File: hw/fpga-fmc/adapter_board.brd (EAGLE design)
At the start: 68.9 x 85.5 mm, 175 parts, among them IC1 M24C02, J1 5569262-1, J2 ASP-134488-01, U1 ADM3066E, U10 ADM3066E, U11 ADM3066E, U12 ADM3066E, U13 ADM3066E, U14 ADM3066E, U15 ADM3066E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

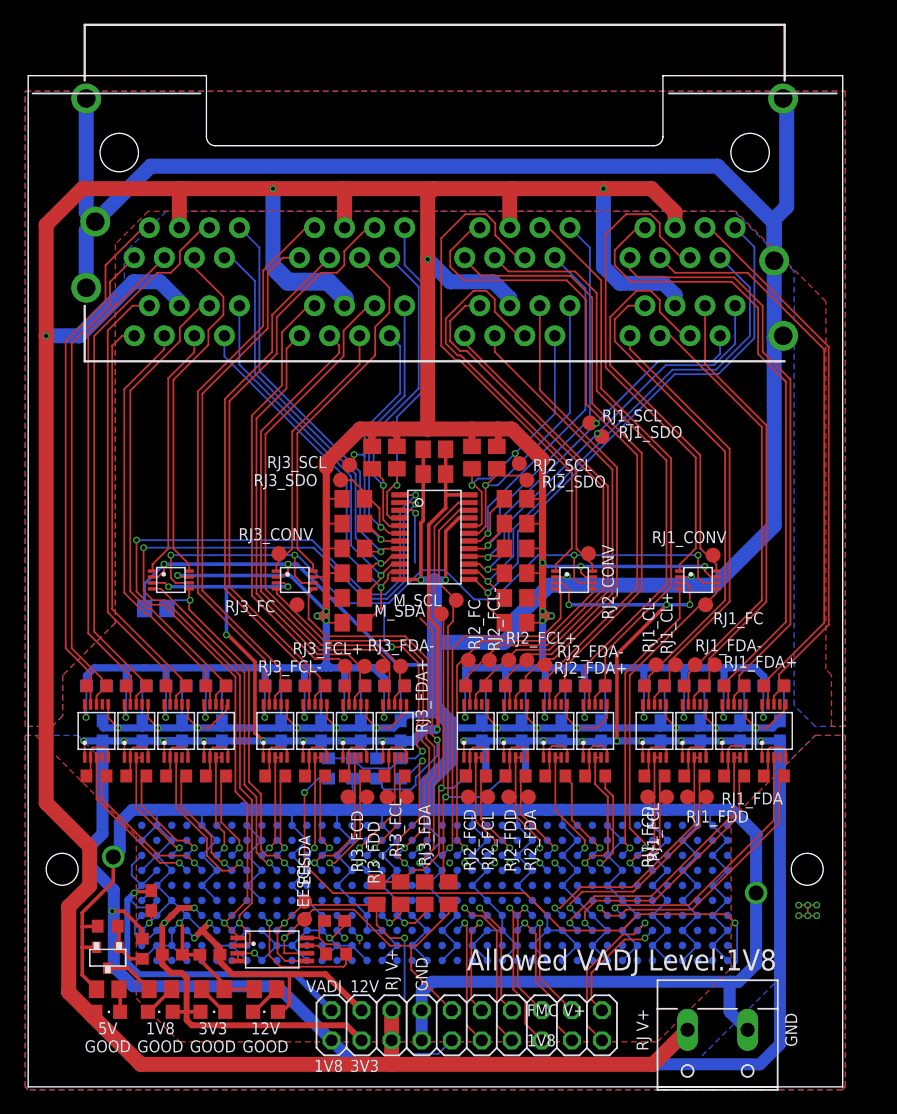
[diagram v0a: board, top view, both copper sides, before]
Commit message: hw/fpga-fmc: reposition i2c switch
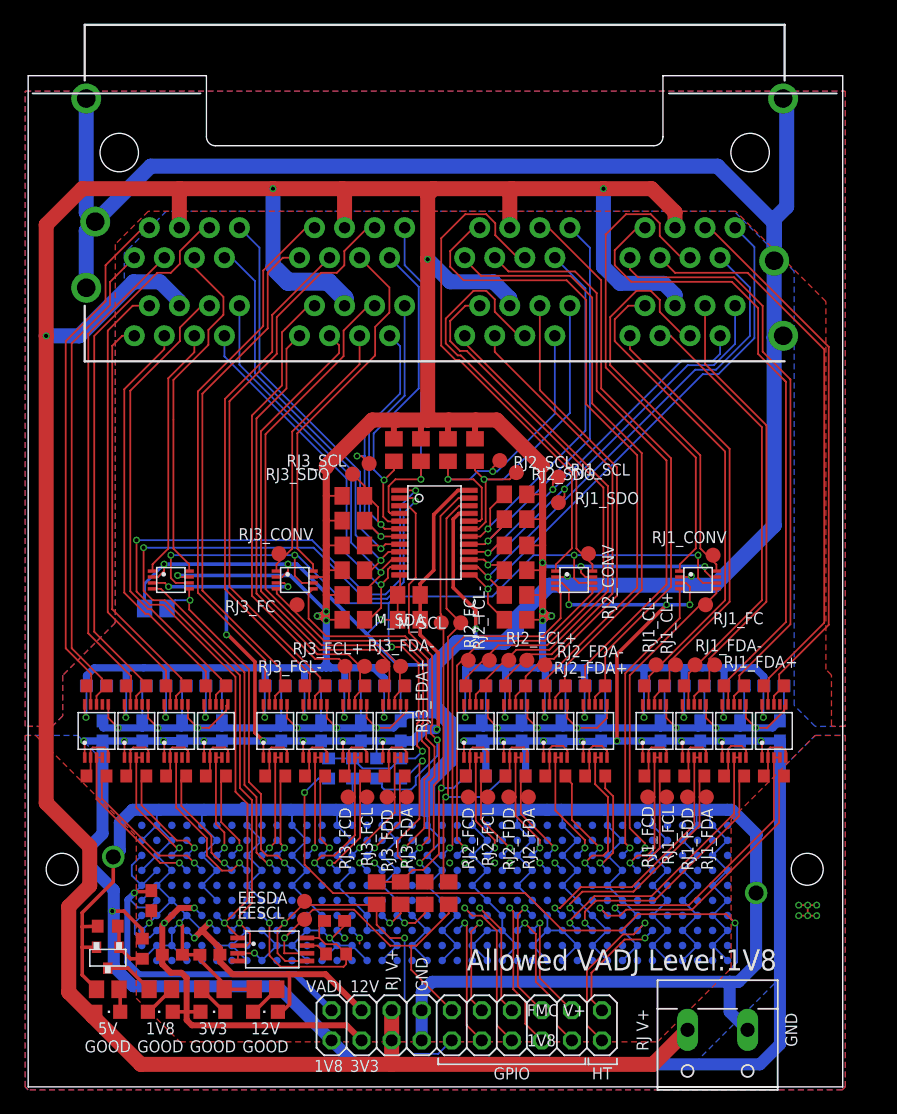
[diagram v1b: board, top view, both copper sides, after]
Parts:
- moved C3 14.6 mm to (32.3, 39.5)
- moved C4 10.4 mm to (32.3, 41.6)
- moved RJ1_SDO 6.69 mm to (45.0, 49.4)
- moved RJ1_SCL 5.29 mm to (45.0, 51.6)
- moved R21 2.13 mm to (35.6, 53.8)
- moved R3 2.13 mm to (33.3, 53.8)
- moved R4 1.95 mm to (31.1, 53.8)
- moved R20 1.95 mm to (37.9, 53.8)
- moved M_SCL 1.94 mm to (36.7, 39.2)
- moved RJ2_SCL 1.67 mm to (40.0, 53.0)
- moved RJ3_SCL 1.66 mm to (29.0, 52.7)
- moved RJ3_SDO 1.14 mm to (27.6, 51.8)
- moved RJ2_SDO 1.09 mm to (41.4, 51.9)
- moved M_SDA 0.76 mm to (35.1, 39.2)
- moved R18 0.38 mm to (41.3, 48.0)
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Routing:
- net 0V: track 811.0 -> 802.8 mm
- net FMC_LA20_P: track 37.2 -> 42.7 mm, vias 3 -> 2
- net RJ2_SCL: track 23.4 -> 27.6 mm
- net 1V8: track 284.1 -> 280.6 mm
- net CONV_OE: track 87.9 -> 85.7 mm
- net RJ5_SDO: track 48.2 -> 46.6 mm
- net RJ5_SCL: track 43.7 -> 42.3 mm
- net RJ3_SDO: track 28.7 -> 27.6 mm
- net RJ7_SDO: track 28.9 -> 29.7 mm
- net RJ1_SCL: track 33.5 -> 32.8 mm
- net RJ4_SCL: track 32.9 -> 33.5 mm
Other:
- board text added: "GPIO"
- board text added: "HT"

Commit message: hw/fpga-fmc: optimize routing
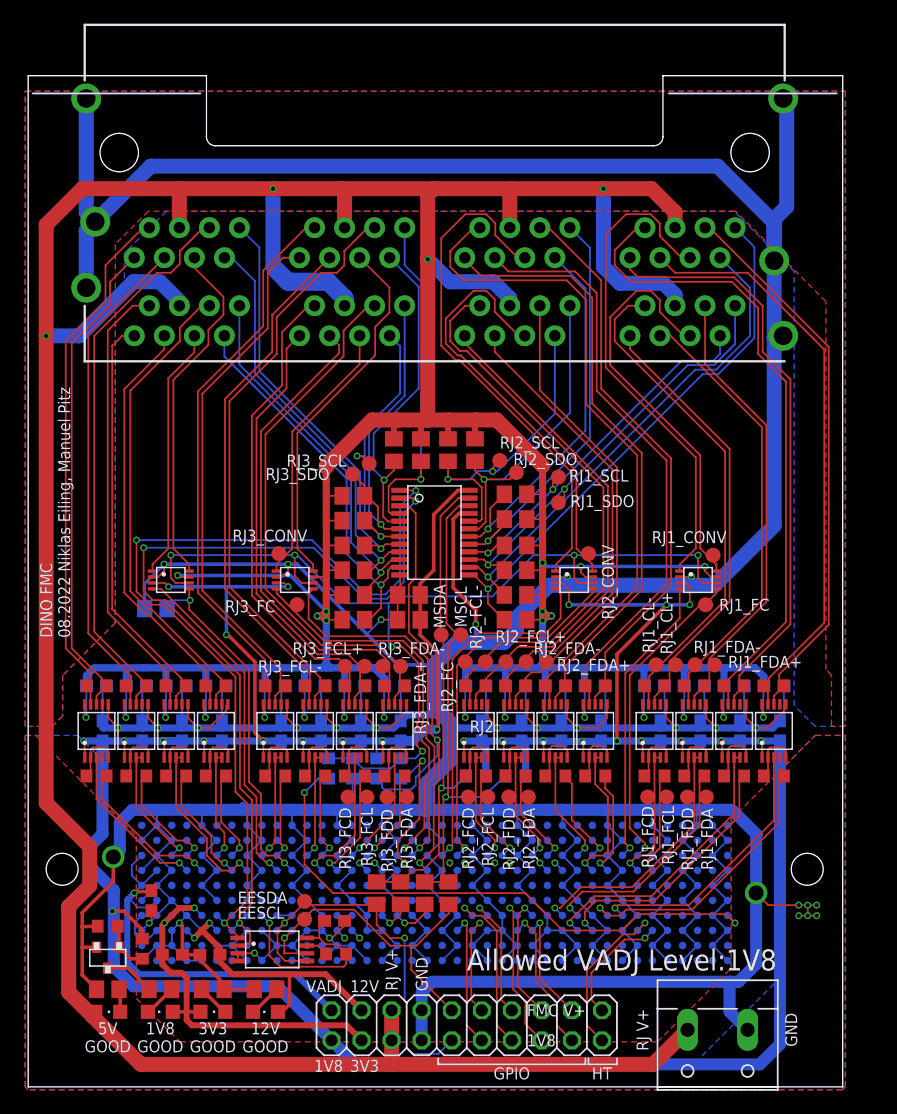
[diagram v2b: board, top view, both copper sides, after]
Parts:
- removed M_SCL, M_SDA: TPB1,27, testpad:B1,27
- added MSCL, MSDA: TPB1,27, testpad:B1,27
- R63, R64: value 0R -> 0R DNP
- R65, R66: value 0R DNP -> 0R
- moved RJ2_FCL- 0.34 mm to (38.8, 35.9), turned to 90 degrees
- moved RJ2_FDA+ 0.28 mm to (43.9, 35.9)
- moved RJ2_FCL+ 0.28 mm to (40.5, 35.9)
- moved RJ2_FC 0.28 mm to (37.1, 35.9)
- moved RJ2_FDA- 0.14 mm to (42.2, 35.9)
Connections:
- net I2C_SCL: now also MSCL.TP; no longer M_SCL.TP
- net I2C_SDA: now also MSDA.TP; no longer M_SDA.TP
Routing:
- net 0V: track 802.8 -> 811.1 mm
- net 1V8_POWER_GOOD: track 53.4 -> 49.1 mm
- net I2C_SCL: track 40.1 -> 42.2 mm
- net FMC_TDI_TDO: track 0.00 -> 1.27 mm
- net 5V: track 524.8 -> 523.7 mm
- net RJ7_DATA_N: track 45.3 -> 44.7 mm
- net LSIO5: track 5.20 -> 4.63 mm
- net RJ7_CLK_N: track 47.9 -> 47.3 mm
- net FMC_LA15_N: track 30.7 -> 30.2 mm
- net FMC_LA31_P: track 13.8 -> 14.3 mm
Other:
- board text added: "DINO FMC 08.2022 Niklas Eiling, Manuel Pitz"
- board text added: "RJ2"

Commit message: hw/fmc minor cleanup in layout and schematic
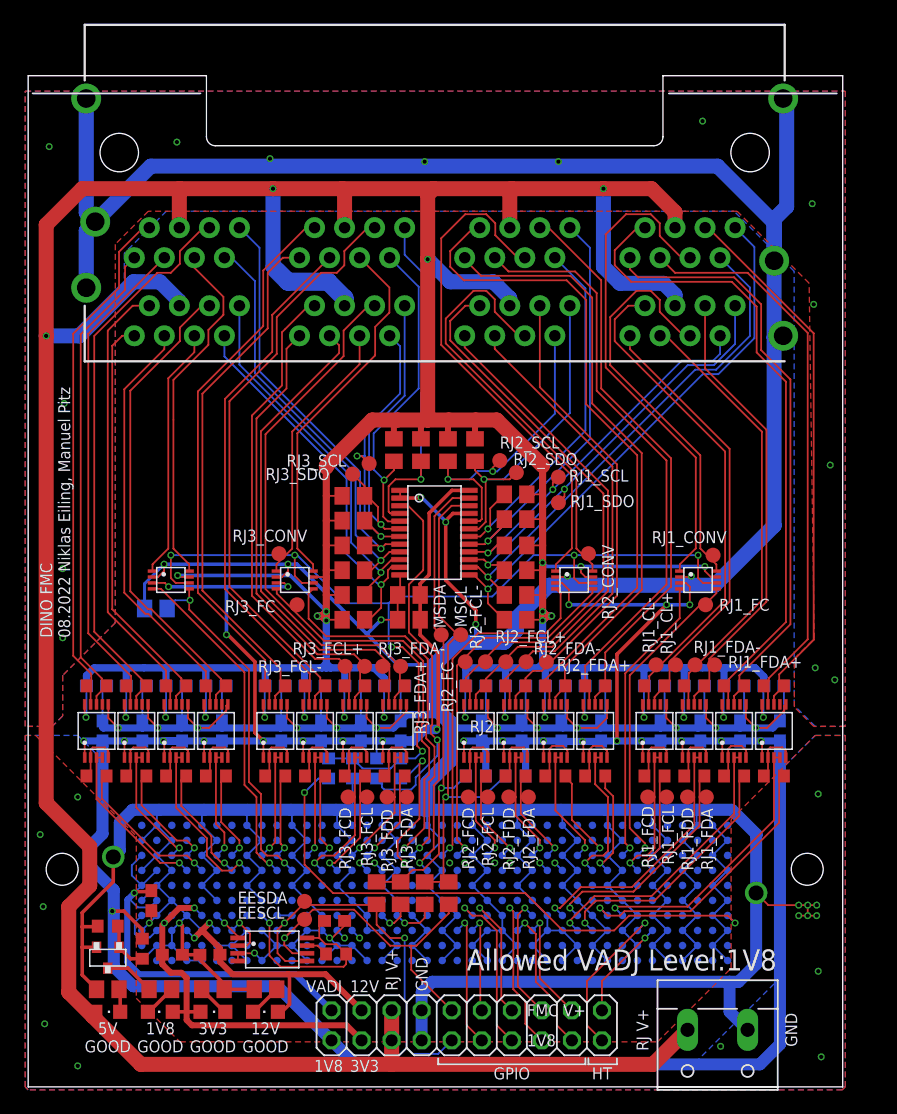
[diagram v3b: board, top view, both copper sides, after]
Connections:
- net 0V: now also U17.P0, U17.P1
- net GA0: no longer U17.P1
- net GA1: no longer U17.P0
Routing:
- net GA1: track 74.5 -> 2.66 mm, vias 3 -> 1
- net GA0: track 73.7 -> 4.05 mm, vias 3 -> 1
- net 0V: track 811.1 -> 813.4 mm, vias 28 -> 53
- net FMC_DP0_M2C_P: track 10.2 -> 8.52 mm
- net 1V8: track 280.7 -> 279.1 mm
- net RJ5_DATA_N: track 49.4 -> 48.2 mm
- net RJ5_DATA_P: track 47.1 -> 46.0 mm
- net I2C_SCL: track 42.2 -> 43.1 mm
- net I2C_SDA: track 40.6 -> 41.3 mm
- net RJ8_CLK_P: track 41.5 -> 40.9 mm
- net FMC_LA14_P: track 8.95 -> 8.35 mm
- net FMC_LA20_P: track 42.7 -> 43.2 mm
- net RJ8_CLK_N: track 44.7 -> 44.2 mm
- net FMC_DP0_M2C_N: track 13.9 -> 13.4 mm

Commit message: hw/fpga-fmc: align GND vias
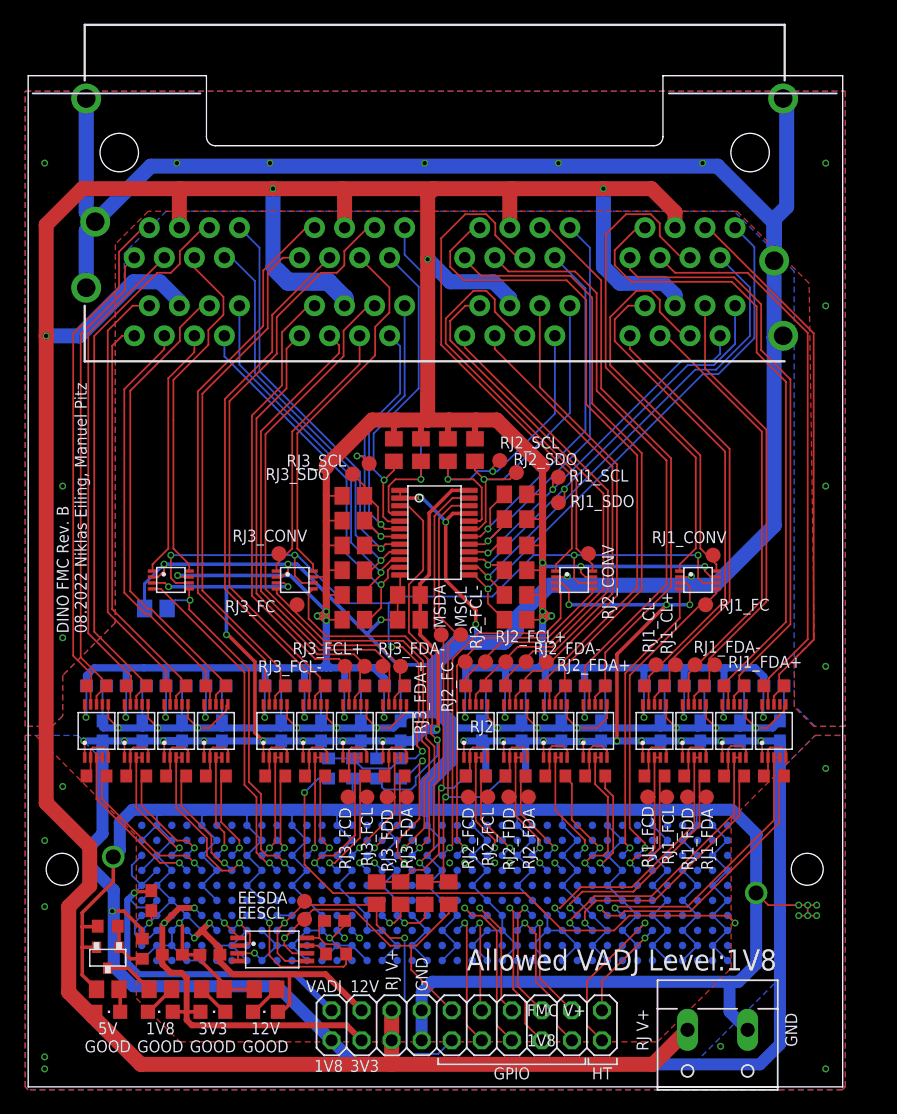
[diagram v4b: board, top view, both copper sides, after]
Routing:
- net 0V: vias 53 -> 50
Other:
- board text added: "DINO FMC Rev. B 08.2022 Niklas Eiling, Manuel Pitz"
- board text removed: "DINO FMC 08.2022 Niklas Eiling, Manuel Pitz"
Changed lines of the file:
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@@
 <wire x1="47.498" y1="1.905" x2="49.911" y2="1.905" width="0.1524" layer="21"/>
 <wire x1="49.911" y1="1.905" x2="49.911" y2="2.413" width="0.1524" layer="21"/>
-<text x="1.143" y="37.973" size="1.016" layer="21" rot="R90" align="top-left">DINO FMC
+<text x="2.54" y="38.354" size="1.016" layer="21" rot="R90" align="top-left">DINO FMC Rev. B
 08.2022 Niklas Eiling, Manuel Pitz</text>
 <text x="38.481" y="30.48" size="1.016" layer="21" rot="R180" align="center">RJ2</text>
@@
 <wire x1="35.433" y1="47.8155" x2="33.401" y2="49.8475" width="0.3048" layer="16"/>
 <via x="35.433" y="47.752" extent="1-16" drill="0.35"/>
-<via x="1.524" y="5.334" extent="1-16" drill="0.35"/>
-<via x="4.318" y="1.778" extent="1-16" drill="0.35"/>
-<via x="1.397" y="15.24" extent="1-16" drill="0.35"/>
-<via x="1.143" y="21.336" extent="1-16" drill="0.35"/>
-<via x="4.318" y="24.511" extent="1-16" drill="0.35"/>
-<via x="3.048" y="43.815" extent="1-16" drill="0.35"/>
+<via x="1.524" y="2.54" extent="1-16" drill="0.35"/>
+<via x="1.524" y="1.524" extent="1-16" drill="0.35"/>
+<via x="1.524" y="15.24" extent="1-16" drill="0.35"/>
+<via x="1.524" y="20.828" extent="1-16" drill="0.35"/>
+<via x="3.048" y="25.4" extent="1-16" drill="0.35"/>
 <via x="3.048" y="37.973" extent="1-16" drill="0.35"/>
-<via x="3.175" y="57.785" extent="1-16" drill="0.35"/>
-<via x="1.905" y="79.502" extent="1-16" drill="0.35"/>
-<via x="12.7" y="79.883" extent="1-16" drill="0.35"/>
-<via x="20.574" y="78.486" extent="1-16" drill="0.35"/>
-<via x="33.655" y="78.232" extent="1-16" drill="0.35"/>
-<via x="44.958" y="78.232" extent="1-16" drill="0.35"/>
-<via x="57.15" y="81.661" extent="1-16" drill="0.35"/>
-<via x="66.421" y="74.676" extent="1-16" drill="0.35"/>
-<via x="68.326" y="34.417" extent="1-16" drill="0.35"/>
-<via x="66.675" y="35.433" extent="1-16" drill="0.35"/>
-<via x="67.945" y="52.578" extent="1-16" drill="0.35"/>
-<via x="66.548" y="66.167" extent="1-16" drill="0.35"/>
-<via x="66.929" y="9.779" extent="1-16" drill="0.35"/>
-<via x="66.929" y="24.765" extent="1-16" drill="0.35"/>
-<via x="67.183" y="2.54" extent="1-16" drill="0.35"/>
+<via x="3.048" y="50.8" extent="1-16" drill="0.35"/>
+<via x="1.524" y="78.105" extent="1-16" drill="0.35"/>
+<via x="12.7" y="78.105" extent="1-16" drill="0.35"/>
+<via x="20.574" y="78.105" extent="1-16" drill="0.35"/>
+<via x="33.655" y="78.105" extent="1-16" drill="0.35"/>
+<via x="44.958" y="78.105" extent="1-16" drill="0.35"/>
+<via x="57.15" y="78.105" extent="1-16" drill="0.35"/>
+<via x="67.564" y="78.105" extent="1-16" drill="0.35"/>
+<via x="67.564" y="35.56" extent="1-16" drill="0.35"/>
+<via x="67.564" y="50.8" extent="1-16" drill="0.35"/>
+<via x="67.564" y="66.04" extent="1-16" drill="0.35"/>
+<via x="67.564" y="26.924" extent="1-16" drill="0.35"/>
+<via x="67.564" y="1.524" extent="1-16" drill="0.35"/>
 <via x="58.674" y="3.429" extent="1-16" drill="0.35"/>
 </signal>

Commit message: hw/fpga-fmc: make rs485 termination resistors 0805 for better power rating
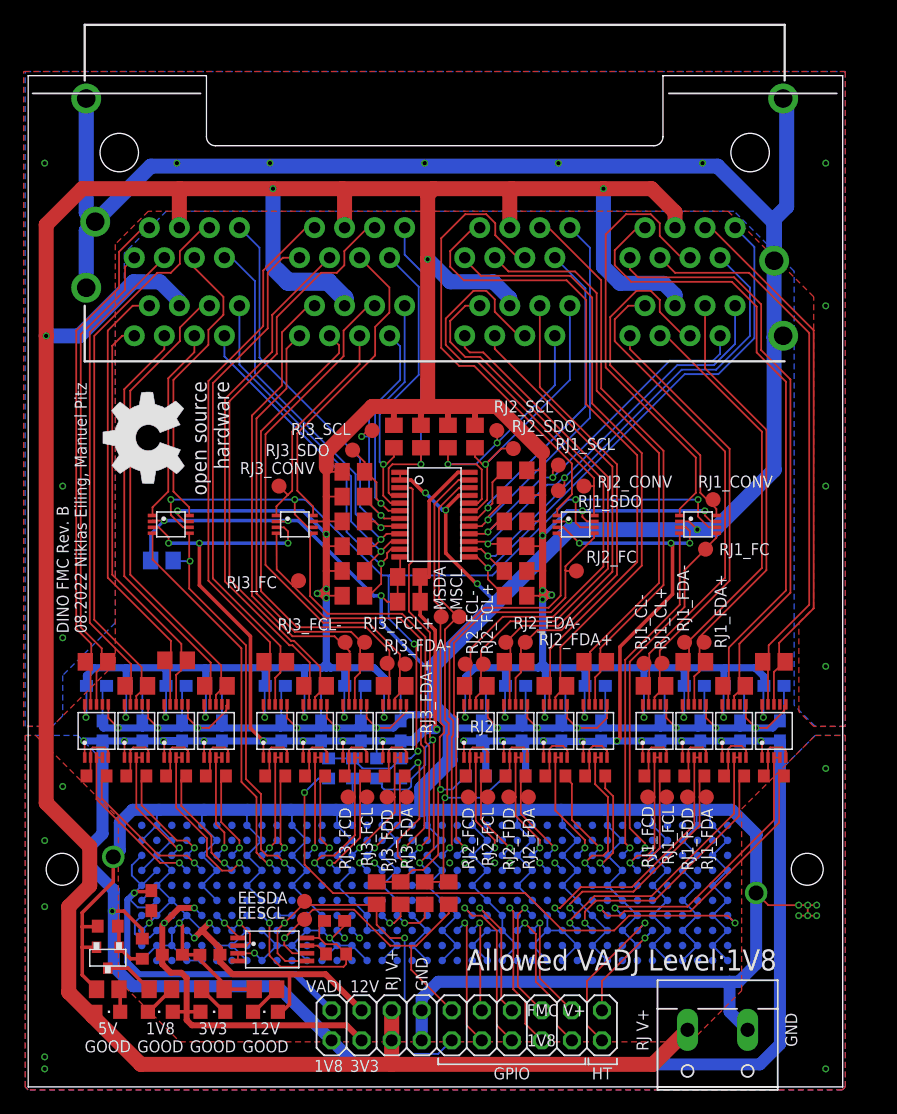
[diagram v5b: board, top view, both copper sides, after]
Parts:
- added U$1: (no value), oshw:OSHW_8MM
- R1, R22, R24, R26, R28, R30, R32, R34, R36, R38, R40, R42, R44, R46, R48, R50: device rcl:R0603 -> rcl:R0805
- moved RJ2_FC 12.1 mm to (46.5, 43.6)
- moved RJ2_CONV 5.73 mm to (47.1, 50.8)
- moved RJ3_CONV 5.71 mm to (21.3, 50.8)
- moved U20 4.70 mm to (46.4, 47.6)
- moved U18 4.70 mm to (12.2, 47.6)
- moved U19 4.70 mm to (22.7, 47.6)
- moved U21 4.70 mm to (56.8, 47.6)
- moved RJ1_CONV 4.70 mm to (58.0, 49.7)
- moved RJ1_FC 4.70 mm to (57.4, 45.5)
- moved R59 4.10 mm to (11.4, 44.5)
- moved RJ3_SCL 2.81 mm to (29.2, 55.5)
- moved RJ2_SCL 2.55 mm to (39.8, 55.5)
- moved RJ2_FDA+ 2.43 mm to (42.2, 37.6)
- moved RJ2_FDA- 2.38 mm to (40.5, 37.6)
- moved R24 2.16 mm to (12.6, 36.1)
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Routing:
- net 1V8: track 279.1 -> 290.8 mm
- net FMC_LA15_P: track 31.2 -> 37.1 mm
- net 0V: track 813.4 -> 808.3 mm, vias 50 -> 49
- net FMC_LA15_N: track 30.2 -> 35.0 mm
- net RJ8_CONV: track 29.8 -> 25.1 mm
- net RJ5_CONV: track 42.2 -> 37.5 mm
- net RJ4_CONV: track 21.4 -> 16.7 mm
- net RJ1_CONV: track 35.4 -> 30.7 mm
- net FMC_LA02_N: track 24.9 -> 29.6 mm
- net RJ7_CONV: track 31.3 -> 26.6 mm
- net FMC_LA02_P: track 26.8 -> 31.1 mm
- net FMC_LA29_N: track 28.7 -> 33.0 mm
- net RJ3_CONV: track 23.3 -> 19.2 mm
- net FMC_LA19_N: track 33.6 -> 37.7 mm
- net RJ6_CONV: track 43.3 -> 39.3 mm
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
